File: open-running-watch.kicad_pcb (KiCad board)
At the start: 4 copper layers, 41 x 61.9 mm, 208 parts, among them IC1 BLUENRG-232N, IC10 NXB0108BQX, IC11 STM32L475RGT6, IC12 W25N512GVEIG, IC13 TPS613222ADBVR, IC14 INA186A5IYFDR, IC15 INA186A5IYFDR, IC16 INA186A5IYFDR, IC17 INA186A5IYFDR, IC18 PCAL9538ABSHP, IC19 INA186A5IYFDR, IC2 TESEO-LIV3F, IC20 INA186A5IYFDR, IC21 LSF0204GU12X, IC22 INA186A5IYFDR, IC3 BGA_725L6_E6327, IC4 BQ27441DRZR-G1A, IC5 MCP73811T-420I_OT, IC6 TPS62237DRYR, IC7 ST1S15J18R, IC8 TLV9002SIRUGR, IC9 ICP-10100, J1 20021121-00014T4LF, J2 10118192-0001LF, J3 1-2328702-0, J4 2328702-4, Q1 BC847BS, Q2 BC847BS, Q3 BC817-25-QVL, Q4 BC847, T1 BALF-NRG-02D3, U1 TPS62233DRYR, Y1 ECS-320-12-37B2-7KM-TR, Y2 NX3215SA-32.768K-EXS00A-MU000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, Y3 ECS-.327-7-1210-TR

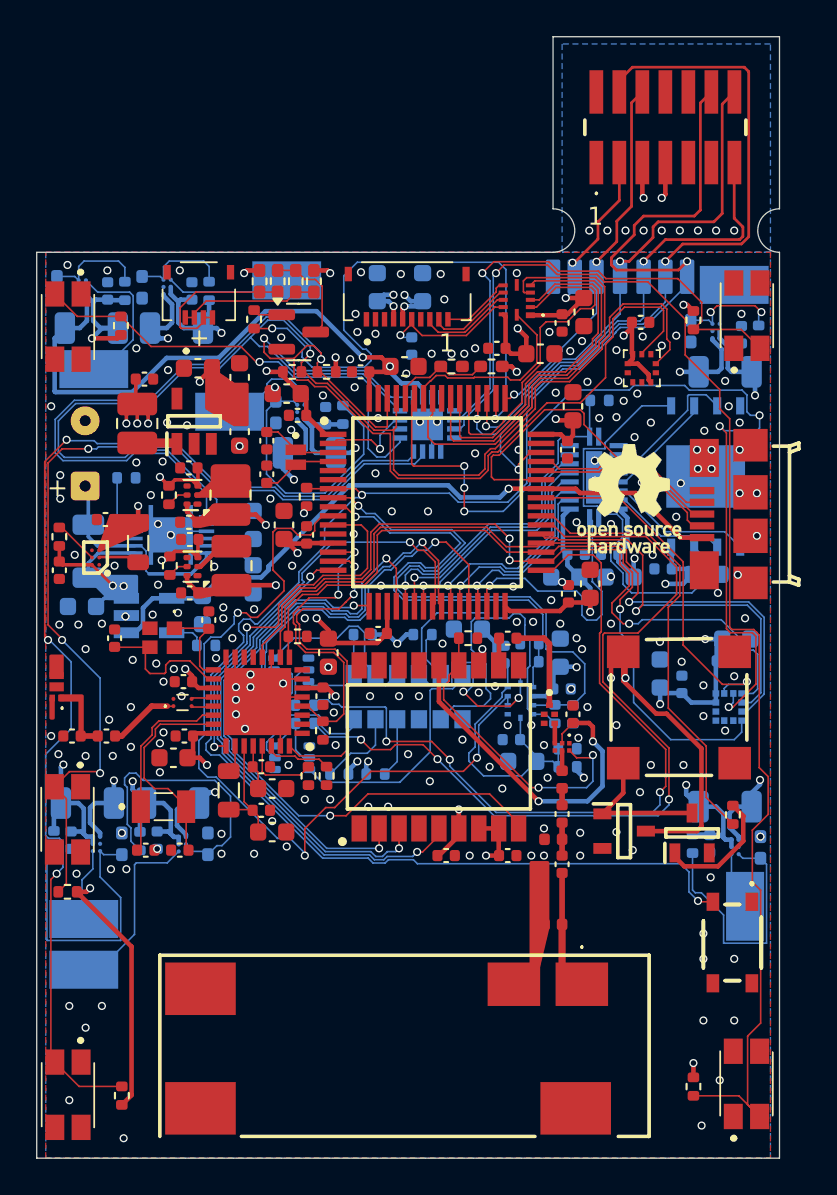
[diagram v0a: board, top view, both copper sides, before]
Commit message: Updated PCB to reflect schematic changes since v0.1.0
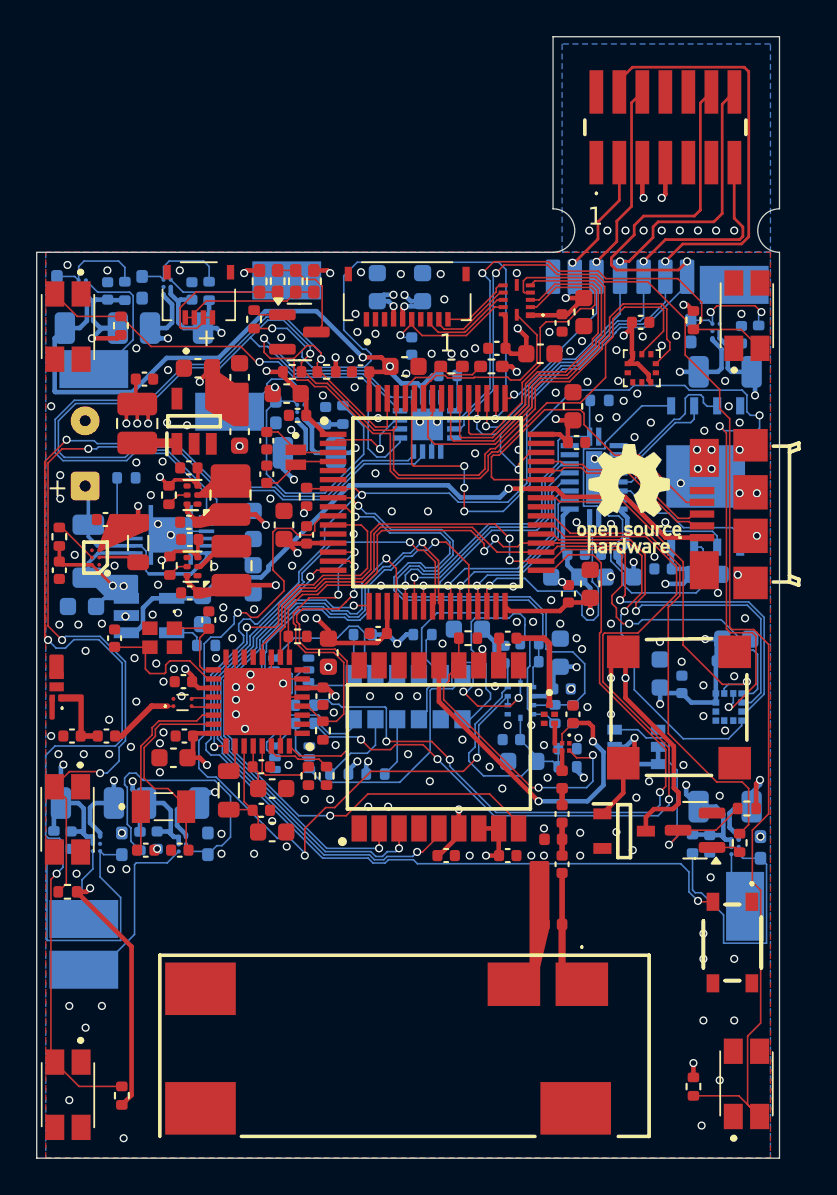
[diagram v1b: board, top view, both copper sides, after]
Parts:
- added Q5: BC846, Package_TO_SOT_SMD:SOT-23, F.Cu at (165.8, 105.9)
- added R64: 10k, Resistor_SMD:R_0402_1005Metric, F.Cu at (168.3, 106.6)
- added R65: 10k, Resistor_SMD:R_0402_1005Metric, B.Cu at (152.2, 80.8)
- Q3: value BC817-25-QVL -> PMN280ENEAX; footprint BC817-25-QVL:SOT95P230X110-3N -> PMN280ENEAX:PMN280ENEAX; moved to B.Cu
- Q4: value BC847 -> BC846
- R49: value 240 -> 10k
- moved Q3 5.66 mm to (162.6, 101.3), turned to 0 degrees
- moved R49 0.85 mm to (168.7, 104.7), turned to 0 degrees
- moved C52 0.64 mm to (159.3, 84.5), turned to 0 degrees
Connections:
- net /controller/OTG_FS_DM renamed /controller/OTG_FS_D-
- net /controller/OTG_FS_DP renamed /controller/OTG_FS_D+
- IC11 pad 35: /accelerometer/SDIO -> /accelerometer/SDO
- IC11 pad 36: /accelerometer/SDO -> /accelerometer/SDIO
- IC18 pad 1: unconnected-(IC18-~{RESET}-Pad1) -> Net-(IC18-~{RESET})
- LED1 pad 1: GND -> /biometric/PD_RG
- LED1 pad 10: /biometric/PD_IR -> GND
- LED1 pad 2: /biometric/PD_RG -> GND
- LED1 pad 3: GND -> /biometric/PD_IR
- Q3 pad 1: Net-(Q3-B) -> Net-(D1-A)
- Q3 pad 2: GND -> Net-(D1-A)
- Q3 pad 3: Net-(D1-A) -> Net-(Q3-G)
- R49 pad 1: /audio/IN -> Net-(Q3-G)
- R49 pad 2: Net-(Q3-B) -> /audio/VCC
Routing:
- net Net-(Q3-G): track 0.00 -> 14.3 mm, vias 0 -> 1
- net Net-(Q3-B): track 6.99 -> 0.00 mm
- net GND: track 28.7 -> 35.4 mm, vias 216 -> 217
- net Net-(IC18-P5): track 63.0 -> 69.3 mm
- net /biometric/PD_IR: track 18.8 -> 13.4 mm
- net Net-(IC18-P4): track 51.1 -> 54.0 mm
- net Net-(D1-A): track 8.24 -> 10.7 mm, vias 0 -> 1
- net /audio/VCC: track 29.4 -> 27.1 mm
- net Net-(IC18-~{RESET}): track 0.00 -> 2.02 mm
- net /audio/IN: track 24.8 -> 26.7 mm
- net /controller/VDD: track 64.8 -> 66.6 mm
- net Net-(Q5-B): track 0.00 -> 1.63 mm
- net /biometric/PD_RG: track 18.2 -> 17.0 mm
- net /accelerometer/SDIO: track 41.7 -> 42.7 mm, vias 1 -> 3
- net /biometric/VOUT_RG: track 31.7 -> 30.8 mm
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
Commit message: Bumped PCB version number to 0.1.1 and updated issue date
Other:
- board text added: "v0.1.1"
- board text removed: "v0.1.0"
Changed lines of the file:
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@@
 	(title_block
 		(title "Open Running Watch")
-		(date "2024-04-12")
-		(rev "0.1.0")
+		(date "2024-05-13")
+		(rev "0.1.1")
 		(company "github.com/fuad1502/open-running-watch-hw")
 	)
@@
 		(tags "resistor")
 		(property "Reference" "R64"
-			(at 0 -1.17 270)
+			(at 0 -1.17 -90)
 			(layer "F.SilkS")
 			(hide yes)
@@
 		)
 		(property "Value" "10k"
-			(at 0 1.17 270)
+			(at 0 1.17 -90)
 			(layer "F.Fab")
 			(effects
@@
 		)
 		(fp_text user "${REFERENCE}"
-			(at 0 0 270)
+			(at 0 0 -90)
 			(layer "F.Fab")
 			(effects
@@
 		(tags "capacitor")
 		(property "Reference" "C52"
-			(at 0 -1.16 360)
+			(at 0 -1.16 0)
 			(layer "F.SilkS")
 			(hide yes)
@@
 		)
 		(property "Value" "100n"
-			(at 0 1.16 360)
+			(at 0 1.16 0)
 			(layer "F.Fab")
 			(effects
@@
 		)
 		(fp_text user "${REFERENCE}"
-			(at 0 0 360)
+			(at 0 0 0)
 			(layer "F.Fab")
 			(effects
@@
 		(tags "resistor")
 		(property "Reference" "R49"
-			(at 0 -1.17 360)
+			(at 0 -1.17 0)
 			(layer "F.SilkS")
 			(hide yes)
@@
 		)
 		(property "Value" "10k"
-			(at 0 1.17 360)
+			(at 0 1.17 0)
 			(layer "F.Fab")
 			(effects
@@
 		)
 		(fp_text user "${REFERENCE}"
-			(at 0 0 360)
+			(at 0 0 0)
 			(layer "F.Fab")
 			(effects
@@
 		(tags "resistor")
 		(property "Reference" "R65"
-			(at 0 1.17 360)
+			(at 0 1.17 0)
 			(layer "B.SilkS")
 			(hide yes)
@@
 		)
 		(property "Value" "10k"
-			(at 0 -1.17 360)
+			(at 0 -1.17 0)
 			(layer "B.Fab")
 			(effects
@@
 		)
 		(fp_text user "${REFERENCE}"
-			(at 0 0 360)
+			(at 0 0 0)
 			(layer "B.Fab")
 			(effects
@@
 		(tags "MOSFET (N-Channel)")
 		(property "Reference" "Q3"
-			(at 0 0 360)
+			(at 0 0 0)
 			(layer "B.SilkS")
 			(hide yes)
@@
 		)
 		(property "Value" "PMN280ENEAX"
-			(at 0 0 360)
+			(at 0 0 0)
 			(layer "B.SilkS")
 			(hide yes)
@@
 		)
 		(fp_text user "${REFERENCE}"
-			(at 0 0 360)
+			(at 0 0 0)
 			(layer "B.Fab")
 			(effects
@@
 		)
 	)
-	(gr_text "v0.1.0"
+	(gr_text "v0.1.1"
 		(locked yes)
-		(at 170 123.6 -0)
+		(at 170 123.6 0)
 		(layer "B.SilkS")
 		(effects
